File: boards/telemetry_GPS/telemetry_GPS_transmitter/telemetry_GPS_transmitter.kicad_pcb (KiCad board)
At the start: 2 copper layers, 98 x 65.5 mm, 69 parts, among them J1 Conn_02x05_Odd_Even, J2 Conn_01x03, J3 Conn_01x03, J4 Conn_Coaxial, J5 54602-908LF, SW1 SW_Push, U1 STM32WL55CCUx, U2 TLV75509PDBV, U3 STLINK-V3MODS, U4 BALFHB-WL-02D3, U5 MASW-007221, U7 NEO-M8N, U8 ISO1042QDWVQ1, U9 MCP2515-xST

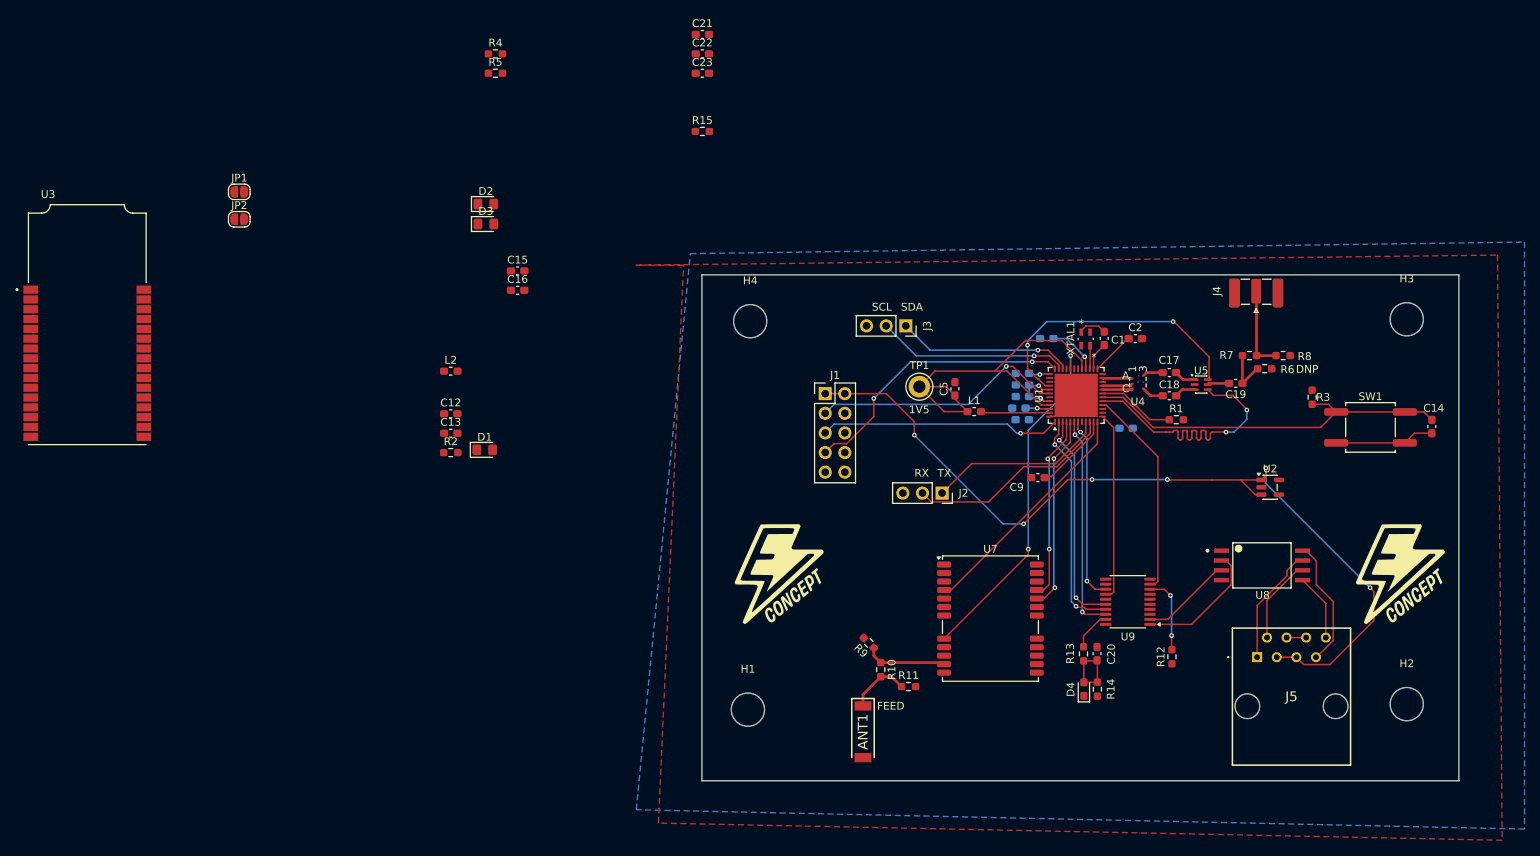
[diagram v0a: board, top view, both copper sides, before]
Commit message: Pushing a finished 2-layer version of the transmitter, will work on 4-layer
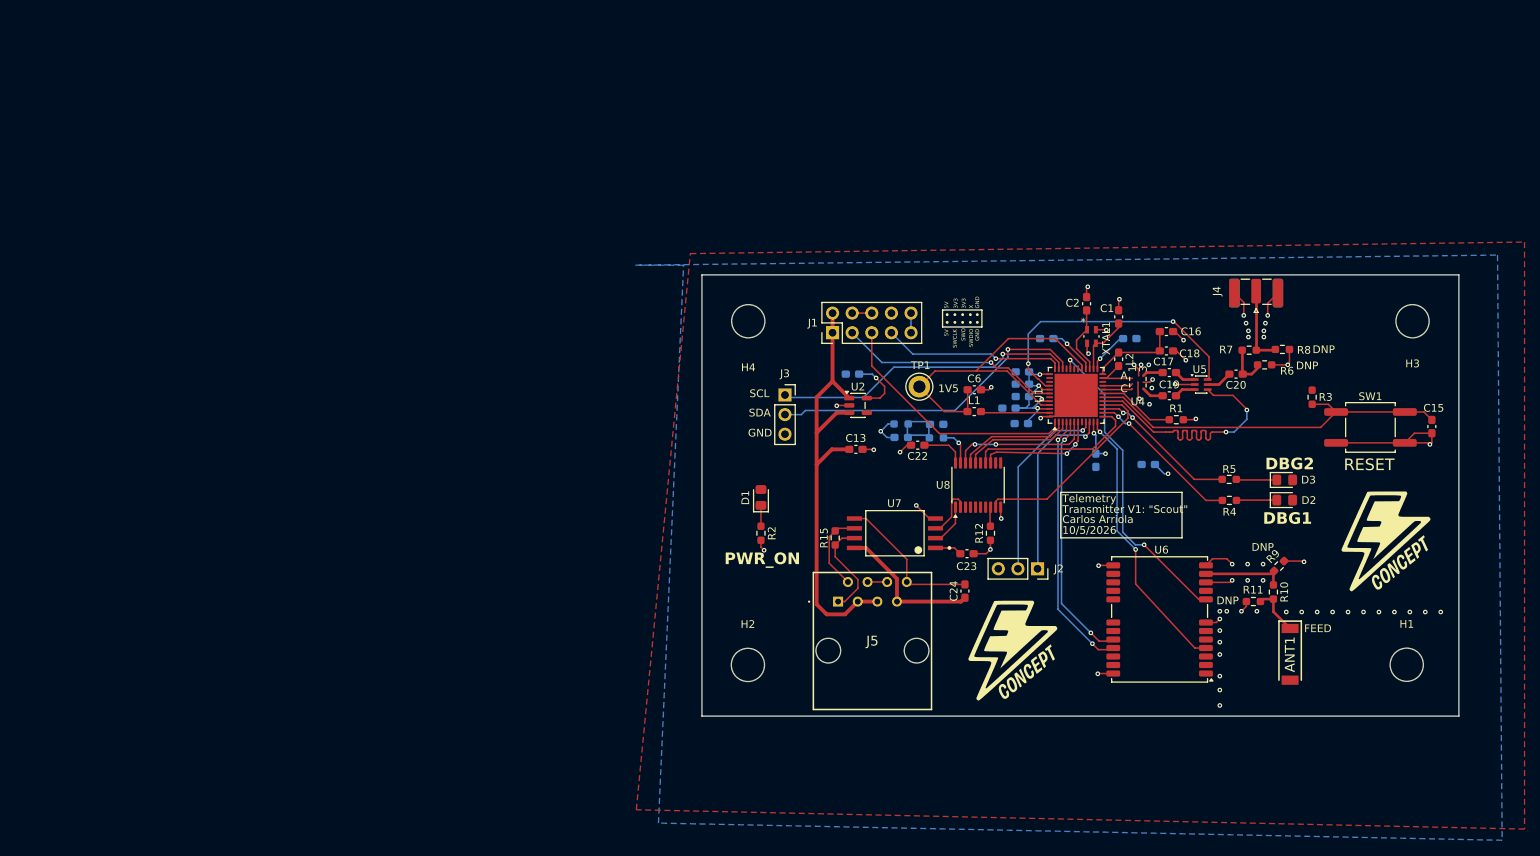
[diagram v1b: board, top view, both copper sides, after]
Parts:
- removed JP1, JP2: SolderJumper_2_Open, Jumper:SolderJumper-2_P1.3mm_Open_RoundedPad1.0x1.5mm
- removed U3: STLINK-V3MODS, STLINK-V3MODS:MODULE_STLINK-V3MODS
- added C2: 6pF, Capacitor_SMD:C_0603_1608Metric_Pad1.08x0.95mm_HandSolder, F.Cu at (161.6, 65.0)
- C1: value 10pF -> 6pF
- C10: renamed from C9; moved to B.Cu
- C14: renamed from C13; moved to B.Cu
- C21: renamed from C20; moved to B.Cu
- C3: renamed from C2; moved to B.Cu
- D4, R13, R14: moved to B.Cu
- moved R4 111.2 mm to (180.0, 90.5), turned to 180 degrees
- moved D2 110.3 mm to (187.2, 90.4)
- moved D3 108.6 mm to (187.2, 87.8)
- moved R5 108.6 mm to (180.0, 87.7), turned to 180 degrees
- moved L2 86.5 mm to (165.7, 72.2), turned to -90 degrees
- moved H1 85.5 mm to (203.0, 111.7)
- moved H2 85.5 mm to (117.7, 111.8)
- moved C16 84.4 mm to (171.9, 68.6)
- moved C17 84.4 mm to (171.9, 71.1)
- moved C24 75.2 mm to (145.8, 102.2), turned to 90 degrees
- moved C23 73.2 mm to (146.1, 97.3)
- moved C22 60.0 mm to (139.7, 83.3), turned to 180 degrees
- moved ANT1 56.2 mm to (187.9, 110.4)
- moved R15 55.4 mm to (129.0, 95.3), turned to 90 degrees
- moved J5 54.7 mm to (129.4, 103.5)
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- renumbered C10 to C11, C11 to C12, C12 to C13, C14 to C15, C15 to C16, C16 to C17, C17 to C18, C18 to C19, C19 to C20, C21 to C22, C22 to C23, C23 to C24, C3 to C4, C4 to C5, C5 to C6, C6 to C7, C7 to C8, C8 to C9, U7 to U6, U8 to U7, U9 to U8
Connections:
- C1 pad 2: Net-(C1-Pad2) -> GND
- J2 pad 1: /Debug/MCU_UART_TX -> /Debug/MCU_UART_RX
- J2 pad 2: /Debug/MCU_UART_RX -> /Debug/MCU_UART_TX
- J3 pad 1: /Debug/I2C_SDA -> /Debug/I2C_SCL
- J3 pad 2: /Debug/I2C_SCL -> /Debug/I2C_SDA
- XTAL1 pad 1: Net-(C1-Pad2) -> /STM32/OSC_IN
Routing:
- net GND: track 20.0 -> 92.6 mm, vias 0 -> 65
- net +5V: track 113.0 -> 61.0 mm, vias 6 -> 0
- net +3V3: track 35.8 -> 67.0 mm, vias 5 -> 11
- net /Debug/DBG_LED_1: track 0.00 -> 20.2 mm, vias 0 -> 2
- net /Debug/DBG_LED_2: track 0.00 -> 19.2 mm, vias 0 -> 2
- net /Debug/I2C_SDA: track 22.9 -> 41.6 mm
- net /CAN/SLAVE_O: track 29.2 -> 14.6 mm, vias 2 -> 0
- net /Debug/I2C_SCL: track 24.9 -> 39.5 mm
- net /CAN/SLAVE_I: track 28.0 -> 14.5 mm, vias 2 -> 0
- net /Debug/SWDIO: track 36.4 -> 23.6 mm, vias 2 -> 1
- net /RF/VR_PA: track 0.00 -> 11.6 mm
- net /CAN/CAN_TX: track 16.7 -> 5.48 mm
- net /CAN/GNDCAN: track 8.69 -> 19.6 mm
- net /GPS/RXD: track 24.0 -> 34.2 mm
- net /CAN/CS_N: track 28.2 -> 18.5 mm
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- added copper zone on F.Cu, net +3V3
- added copper zone on B.Cu, net GND
- removed copper zone on B.Cu, net +3V3
- removed copper zone on F.Cu, net GND
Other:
- board size 98 x 65.5 mm -> 98 x 57.1 mm
- board text added: "10/5/2026"
- board text added: "3V3"
- board text added: "5V"
- board text added: "Carlos Arriola"
- board text added: "DBG1"
- board text added: "DBG2"
- board text added: "GND"
- board text added: "PWR_ON"
- board text added: "RESET"
- board text added: "SWCLK"
- board text added: "SWDIO"
- board text added: "SWO"
- board text added: "Telemetry"
- board text added: "Transmitter V1: {dblquote}Scout{dblquote}"
- board text added: "X"
- board text removed: "RX"
- board text removed: "TX"

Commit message: Pushing 4-layer design, still needs revision
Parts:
- moved C11 1.10 mm to (152.1, 77.0)
- moved C12 1.10 mm to (152.1, 73.8)
- moved C9 1.10 mm to (152.1, 75.4)
- moved J5 0.58 mm to (129.2, 104.1)
- moved R15 0.19 mm to (129.0, 95.5)
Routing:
- net GND: track 92.6 -> 117.1 mm, vias 65 -> 84
- net +3V3: track 67.0 -> 87.7 mm, vias 11 -> 25
- net /CAN/5VCAN: track 19.1 -> 20.1 mm
- net Net-(U6-RF_IN): track 10.7 -> 11.5 mm
- net /CAN/GNDCAN: track 19.6 -> 20.2 mm
- added copper zone on In2.Cu, net +3V3
- added copper zone on In1.Cu, net GND
- removed copper zone on F.Cu, net +3V3
- removed copper zone on B.Cu, net GND
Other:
- copper layers 2 -> 4
- board text added: "RX"
- board text added: "TX"
- board text added: "x"
- board text removed: "X"
